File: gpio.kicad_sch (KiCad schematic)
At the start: 5 parts, among them J1 CONN_02X20, J2 CONN_02X20

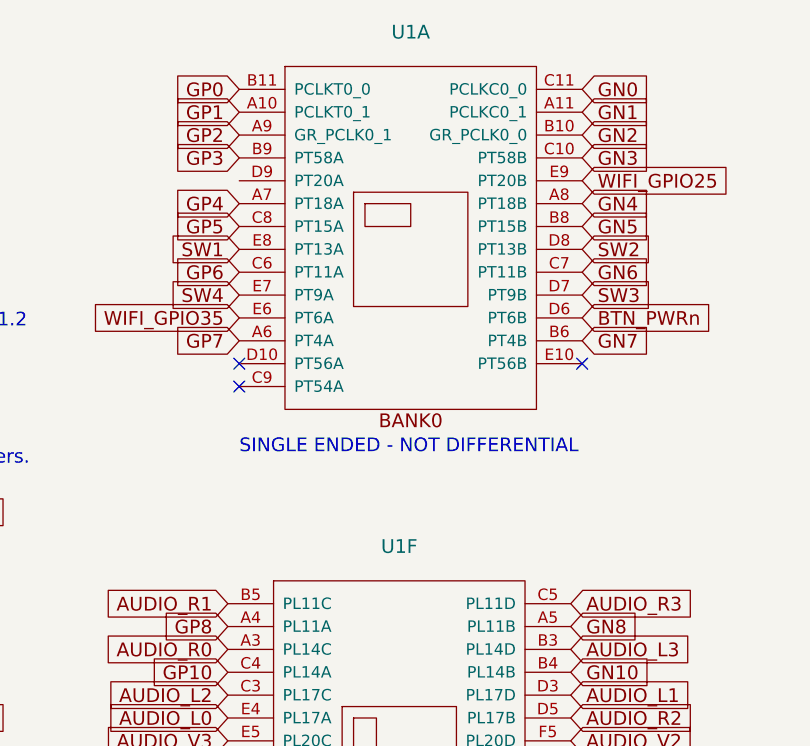
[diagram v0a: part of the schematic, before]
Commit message: Full SerDes is now connected
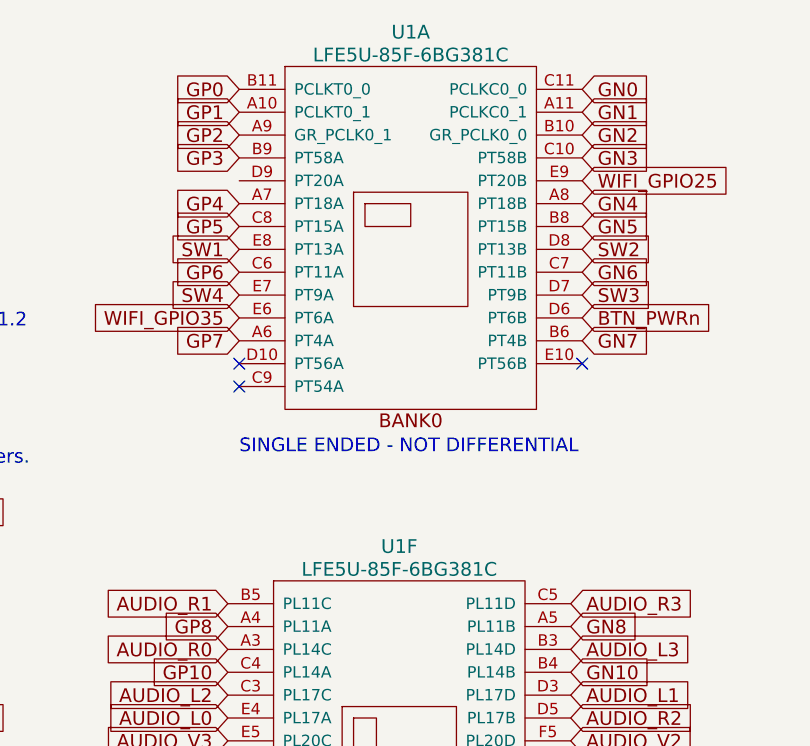
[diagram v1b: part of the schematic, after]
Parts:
- U1: value (none) -> LFE5U-85F-6BG381C; footprint (none) -> lfe5bg381:BGA-381_pitch0.8mm_dia0.4mm; MNF1_URL (none) -> www.latticesemi.com
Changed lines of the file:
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@@
   )
   (symbol (lib_id "lfe5bg381:LFE5UM-85F-6BG381C") (at 125.73 63.5 0) (unit 1)
-    (in_bom yes) (on_board yes)
+    (in_bom yes) (on_board no)
     (property "Reference" "U1" (id 0) (at 125.73 39.37 0)
       (effects (font (size 1.524 1.524)))
     )
-    (property "Value" "" (id 1) (at 125.73 41.91 0)
+    (property "Value" "LFE5U-85F-6BG381C" (id 1) (at 125.73 41.91 0)
       (effects (font (size 1.524 1.524)))
     )
-    (property "Footprint" "" (id 2) (at 99.06 39.37 0)
-      (effects (font (size 1.524 1.524)) hide)
-    )
-    (property "Datasheet" "http://www.latticesemi.com/~/media/LatticeSemi/Documents/DataSheets/ECP5/FPGA-DS-02012.pdf" (id 3) (at 99.06 39.37 0)
+    (property "Footprint" "lfe5bg381:BGA-381_pitch0.8mm_dia0.4mm" (id 2) (at 99.06 39.37 0)
+      (effects (font (size 1.524 1.524)) hide)
+    )
+    (property "Datasheet" "http://www.latticesemi.com/~/media/LatticeSemi/Documents/ApplicationNotes/EH/TN1261.pdf?document_id=50463" (id 3) (at 99.06 39.37 0)
       (effects (font (size 1.524 1.524)) hide)
     )
     (property "MPN" "LFE5U-85F-6BG381C" (id 4) (at 125.73 63.5 0)
+      (effects (font (size 1.524 1.524)) hide)
+    )
+    (property "MNF1_URL" "www.latticesemi.com" (id 5) (at 125.73 63.5 0)
       (effects (font (size 1.524 1.524)) hide)
     )
@@
   )
   (symbol (lib_id "lfe5bg381:LFE5UM-85F-6BG381C") (at 124.46 120.65 0) (unit 6)
-    (in_bom yes) (on_board yes)
+    (in_bom yes) (on_board no)
     (property "Reference" "U1" (id 0) (at 124.46 96.52 0)
       (effects (font (size 1.524 1.524)))
     )
-    (property "Value" "" (id 1) (at 124.46 99.06 0)
+    (property "Value" "LFE5U-85F-6BG381C" (id 1) (at 124.46 99.06 0)
       (effects (font (size 1.524 1.524)))
     )
-    (property "Footprint" "" (id 2) (at 97.79 96.52 0)
-      (effects (font (size 1.524 1.524)) hide)
-    )
-    (property "Datasheet" "http://www.latticesemi.com/~/media/LatticeSemi/Documents/DataSheets/ECP5/FPGA-DS-02012.pdf" (id 3) (at 97.79 96.52 0)
+    (property "Footprint" "lfe5bg381:BGA-381_pitch0.8mm_dia0.4mm" (id 2) (at 97.79 96.52 0)
+      (effects (font (size 1.524 1.524)) hide)
+    )
+    (property "Datasheet" "http://www.latticesemi.com/~/media/LatticeSemi/Documents/ApplicationNotes/EH/TN1261.pdf?document_id=50463" (id 3) (at 97.79 96.52 0)
       (effects (font (size 1.524 1.524)) hide)
     )
@@
       (effects (font (size 1.524 1.524)) hide)
     )
+    (property "MNF1_URL" "www.latticesemi.com" (id 5) (at 124.46 120.65 0)
+      (effects (font (size 1.524 1.524)) hide)
+    )
